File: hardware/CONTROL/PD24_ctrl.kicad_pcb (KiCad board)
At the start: 2 copper layers, 24.8 x 14 mm, 20 parts, among them J1 Conn_01x12_Socket, J2 Conn_01x08_Socket, U2 STM32G031G8Ux, U5 INA228

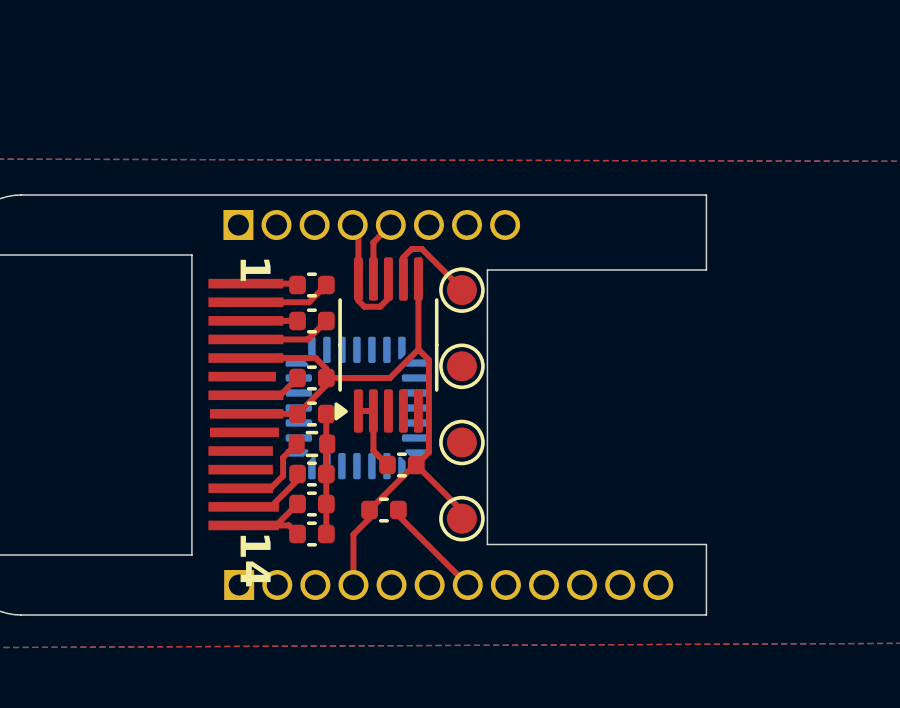
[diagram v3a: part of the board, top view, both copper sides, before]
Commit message: 优化了布局的结构，使其能够在缩小的板框能够单面布局，适合焊接且不影响屏幕贴装
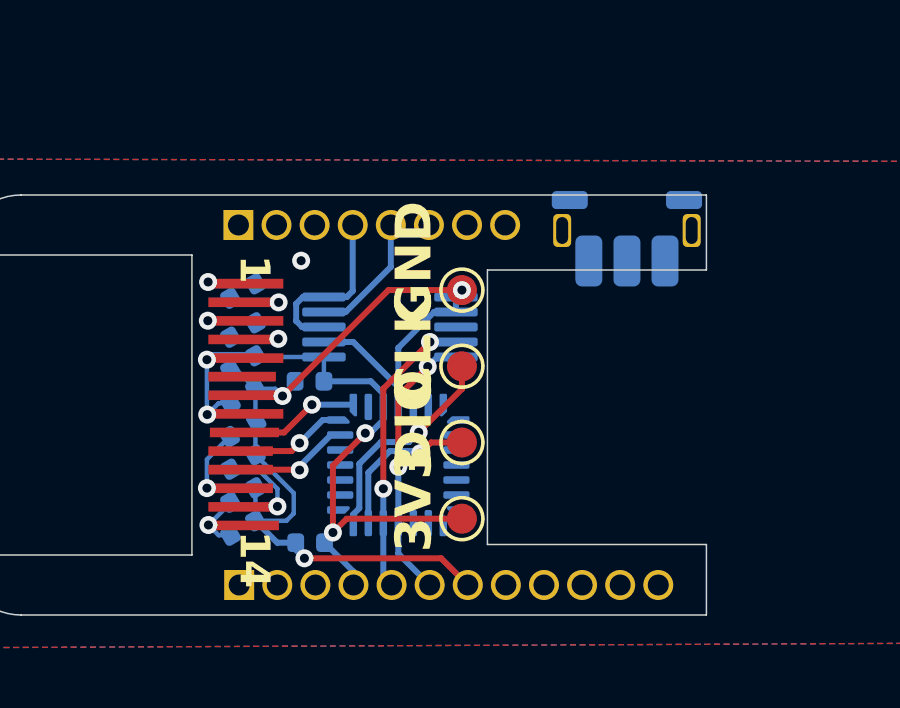
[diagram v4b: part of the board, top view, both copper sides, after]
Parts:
- added REF**: KEY-SMD_3P-L4.3-W3.05, my_footprint:KEY-SMD_3P-L4.3-W3.05, B.Cu at (154.7, 108.5)
- C10, C11, C12, C13, C14, C6, C7, C8, C9, R8, U5: moved to B.Cu
- moved C6 4.16 mm to (144.1, 112.5)
- moved C14 2.69 mm to (144.1, 117.8), turned to 180 degrees
- moved C10 2.38 mm to (141.9, 113.0), turned to 30 degrees
- moved C9 2.35 mm to (141.9, 111.8), turned to -150 degrees
- moved R8 2.35 mm to (141.9, 114.0), turned to -150 degrees
- moved U2 2.35 mm to (147.1, 115.2)
- moved C11 2.33 mm to (141.9, 115.2), turned to 30 degrees
- moved C13 2.32 mm to (141.9, 116.2), turned to 30 degrees
- moved C8 2.32 mm to (141.9, 110.8), turned to 30 degrees
- moved C12 2.31 mm to (141.9, 117.3), turned to 30 degrees
- moved C7 2.31 mm to (141.9, 109.5), turned to 30 degrees
- moved U5 0.60 mm to (146.8, 110.7), turned to 180 degrees
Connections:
- TP2 pad 1: /SWDIO -> /SWCLK
- TP3 pad 1: /SWCLK -> /SWDIO
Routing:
- net GND: track 15.3 -> 33.5 mm, vias 0 -> 4
- net /I2C2.SDA: track 0.00 -> 9.72 mm, vias 0 -> 2
- net /I2C2.SCL: track 0.00 -> 9.19 mm, vias 0 -> 2
- net /SWCLK: track 0.00 -> 7.33 mm, vias 0 -> 1
- net /SWDIO: track 0.00 -> 5.28 mm, vias 0 -> 1
- net /OLED_RST: track 0.00 -> 4.02 mm, vias 0 -> 1
- net /I2C1.SDA: track 0.00 -> 3.88 mm, vias 0 -> 1
- net /I2C1.SCL: track 0.00 -> 3.69 mm, vias 0 -> 1
- net /VIN-: track 2.04 -> 4.25 mm
- net Net-(U12-VCC): track 4.00 -> 1.94 mm, vias 0 -> 1
- net /VIN+: track 4.45 -> 5.84 mm
- net Net-(U12-C1N): track 2.93 -> 1.62 mm, vias 0 -> 1
- net Net-(U12-C2N): track 2.92 -> 1.66 mm, vias 0 -> 1
- net Net-(U12-IREF): track 2.83 -> 2.03 mm, vias 0 -> 1
- net +3V3: track 23.7 -> 23.2 mm, vias 0 -> 4
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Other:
- board text added: "3V3"
- board text added: "CLK"
- board text added: "DIO"
- board text added: "GND"

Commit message: 硬件版本v2，待验证
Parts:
- removed REF**: KEY-SMD_3P-L4.3-W3.05, my_footprint:KEY-SMD_3P-L4.3-W3.05
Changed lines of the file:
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@@
 		(tags "capacitor")
 		(property "Reference" "C6"
-			(at 0 1.16 360)
+			(at 0 1.16 0)
 			(layer "B.SilkS")
 			(hide yes)
@@
 		)
 		(property "Value" "0.1uF"
-			(at 0 -1.16 360)
+			(at 0 -1.16 0)
 			(layer "B.Fab")
 			(effects
@@
 		)
 		(fp_text user "${REFERENCE}"
-			(at 0 0 360)
+			(at 0 0 0)
 			(layer "B.Fab")
 			(effects
@@
 		(tags "capacitor")
 		(property "Reference" "C14"
-			(at 0 1.16 360)
+			(at 0 1.16 0)
 			(layer "B.SilkS")
 			(hide yes)
@@
 		)
 		(property "Value" "0.1uF"
-			(at 0 -1.16 360)
+			(at 0 -1.16 0)
 			(layer "B.Fab")
 			(effects
@@
 		)
 		(fp_text user "${REFERENCE}"
-			(at 0 0 360)
+			(at 0 0 0)
 			(layer "B.Fab")
 			(effects
@@
 			(offset
 				(xyz 0 0 0)
-			)
-			(scale
-				(xyz 1 1 1)
-			)
-			(rotate
-				(xyz 0 0 0)
-			)
-		)
-	)
-	(footprint "my_footprint:KEY-SMD_3P-L4.3-W3.05"
-		(layer "B.Cu")
-		(at 154.7 108.45 180)
-		(property "Reference" "REF**"
-			(at 0 10.39 0)
-			(unlocked yes)
-			(layer "B.SilkS")
-			(effects
-				(font
-					(size 1 1)
-					(thickness 0.15)
-				)
-				(justify mirror)
-			)
-		)
-		(property "Value" "KEY-SMD_3P-L4.3-W3.05"
-			(at 0 8.89 0)
-			(unlocked yes)
-			(layer "B.Fab")
-			(effects
-				(font
-					(size 1 1)
-					(thickness 0.15)
-				)
-				(justify mirror)
-			)
-		)
-		(property "Footprint" "my_footprint:KEY-SMD_3P-L4.3-W3.05"
-			(at 0 9.89 0)
-			(unlocked yes)
-			(layer "B.Fab")
-			(hide yes)
-			(effects
-				(font
-					(size 1 1)
-					(thickness 0.15)
-				)
-				(justify mirror)
-			)
-		)
-		(property "Datasheet" ""
-			(at 0 9.89 0)
-			(unlocked yes)
-			(layer "B.Fab")
-			(hide yes)
-			(effects
-				(font
-					(size 1 1)
-					(thickness 0.15)
-				)
-				(justify mirror)
-			)
-		)
-		(property "Description" ""
-			(at 0 9.89 0)
-			(unlocked yes)
-			(layer "B.Fab")
-			(hide yes)
-			(effects
-				(font
-					(size 1 1)
-					(thickness 0.15)
-				)
-				(justify mirror)
-			)
-		)
-		(attr smd)
-		(fp_rect
-			(start -2.159 2.54)
-			(end 2.159 -0.508)
-			(stroke
-				(width 0.12)
-				(type default)
-			)
-			(fill none)
-			(layer "B.SilkS")
-		)
-		(fp_text user "${REFERENCE}"
-			(at 0 7.39 0)
-			(unlocked yes)
-			(layer "B.Fab")
-			(effects
-				(font
-					(size 1 1)
-					(thickness 0.15)
-				)
-				(justify mirror)
-			)
-		)
-		(pad "1" smd roundrect
-			(at -1.27 0 180)
-			(size 0.9 1.7)
-			(layers "B.Cu" "B.Paste" "B.Mask")
-			(roundrect_rratio 0.25)
-			(thermal_bridge_angle 45)
-		)
-		(pad "2" smd roundrect
-			(at 0 0 180)
-			(size 0.9 1.7)
-			(layers "B.Cu" "B.Paste" "B.Mask")
-			(roundrect_rratio 0.25)
-			(thermal_bridge_angle 45)
-		)
-		(pad "3" smd roundrect
-			(at 1.27 0 180)
-			(size 0.9 1.7)
-			(layers "B.Cu" "B.Paste" "B.Mask")
-			(roundrect_rratio 0.25)
-			(thermal_bridge_angle 45)
-		)
-		(pad "4" smd roundrect
-			(at -1.905 2.032 180)
-			(size 1.2 0.6)
-			(layers "B.Cu" "B.Paste" "B.Mask")
-			(roundrect_rratio 0.25)
-			(thermal_bridge_angle 45)
-		)
-		(pad "5" smd roundrect
-			(at 1.905 2.032 180)
-			(size 1.2 0.6)
-			(layers "B.Cu" "B.Paste" "B.Mask")
-			(roundrect_rratio 0.25)
-			(thermal_bridge_angle 45)
-		)
-		(pad "GND" thru_hole roundrect
-			(at -2.159 1.016 180)
-			(size 0.6 1.1)
-			(drill oval 0.4 0.9)
-			(layers "*.Cu" "*.Mask")
-			(remove_unused_layers no)
-			(roundrect_rratio 0.25)
-			(thermal_bridge_angle 45)
-		)
-		(pad "GND" thru_hole roundrect
-			(at 2.159 1.016 180)
-			(size 0.6 1.1)
-			(drill oval 0.4 0.9)
-			(layers "*.Cu" "*.Mask")
-			(remove_unused_layers no)
-			(roundrect_rratio 0.25)
-			(thermal_bridge_angle 45)
-		)
-		(model "${KICAD_USER_LIB}/model/按键、摇杆/侧按键.STEP"
-			(offset
-				(xyz 0 0 0)

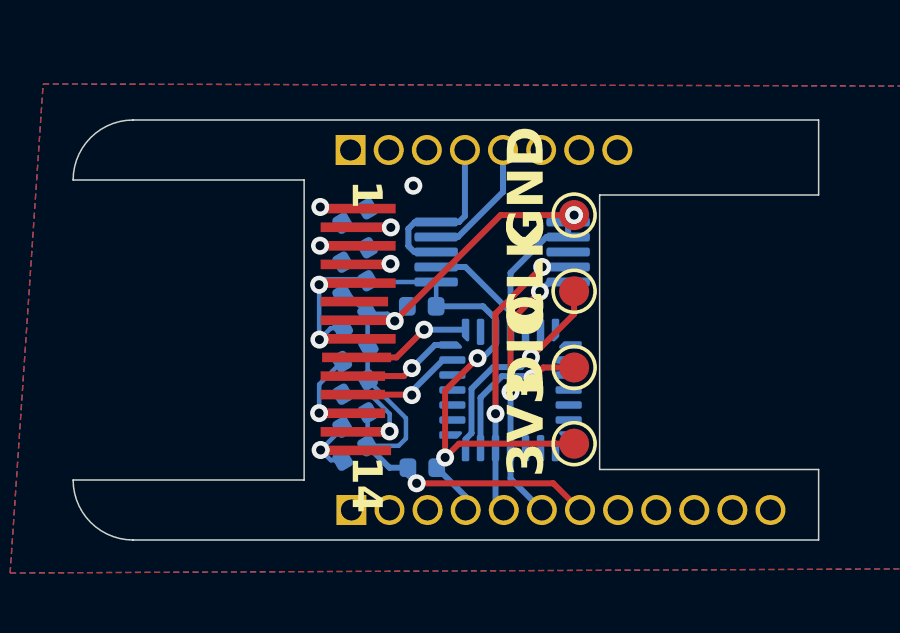
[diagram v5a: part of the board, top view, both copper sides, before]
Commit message: lis2dw12由于错误配置了cs脚，导致进入了spi模式，但电路设计上为iic的连接方式，无法读取方向，现在已经修正，但是代码设置成了固定方向。同步升压整流确实降低了不少发热，但是好像添加的ldo由于oled电流较大，带来的额外热量更多，之后可能还是考虑使用dcdc降压
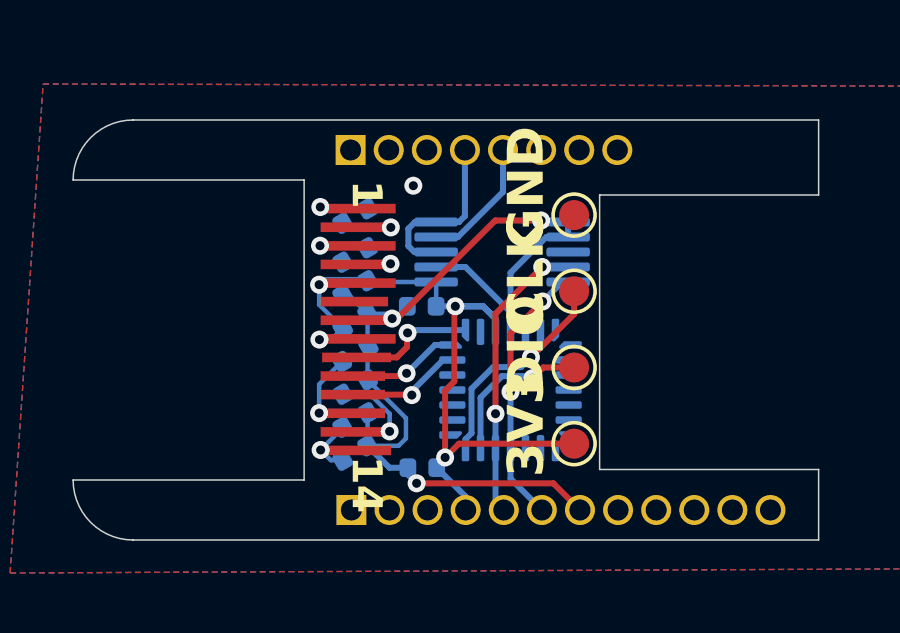
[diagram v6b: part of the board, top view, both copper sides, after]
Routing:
- net +3V3: track 23.2 -> 25.3 mm
- net GND: track 33.5 -> 32.2 mm
